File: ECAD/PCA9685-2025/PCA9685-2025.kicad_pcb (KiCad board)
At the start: 2 copper layers, 58 x 38 mm, 80 parts, among them J1 Conn_01x03, J10 Conn_01x03, J11 Conn_01x03, J12 Conn_01x03, J13 Conn_01x03, J14 Conn_01x03, J15 Conn_01x03, J16 Conn_01x03, J17 Conn_01x03, J18 Conn_01x04, J19 Conn_01x04, J2 Conn_01x02, J3 Conn_01x03, J4 Conn_01x03, J5 Conn_01x03, J6 Conn_01x03, J7 Conn_01x03, J8 Conn_01x03, J9 Conn_01x03, U1 PCA9685PW

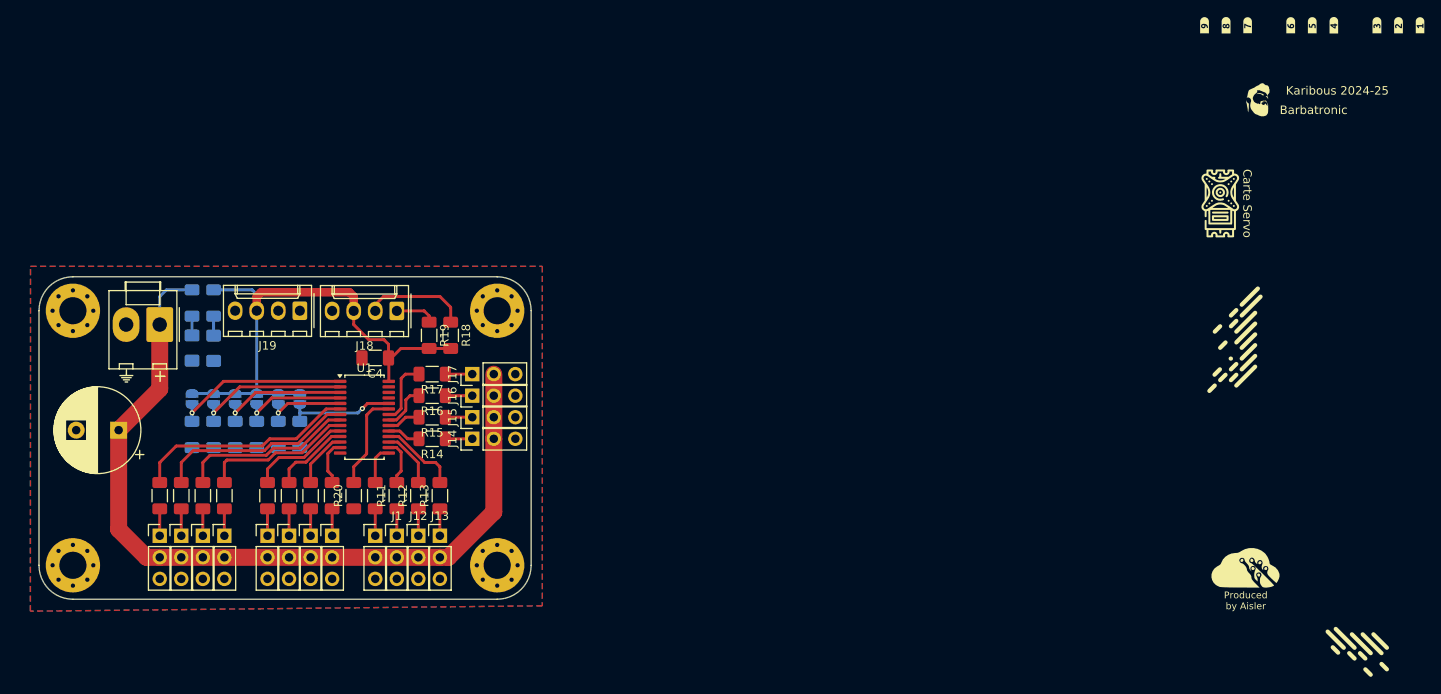
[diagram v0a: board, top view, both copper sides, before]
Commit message: finish route and update silkscreen
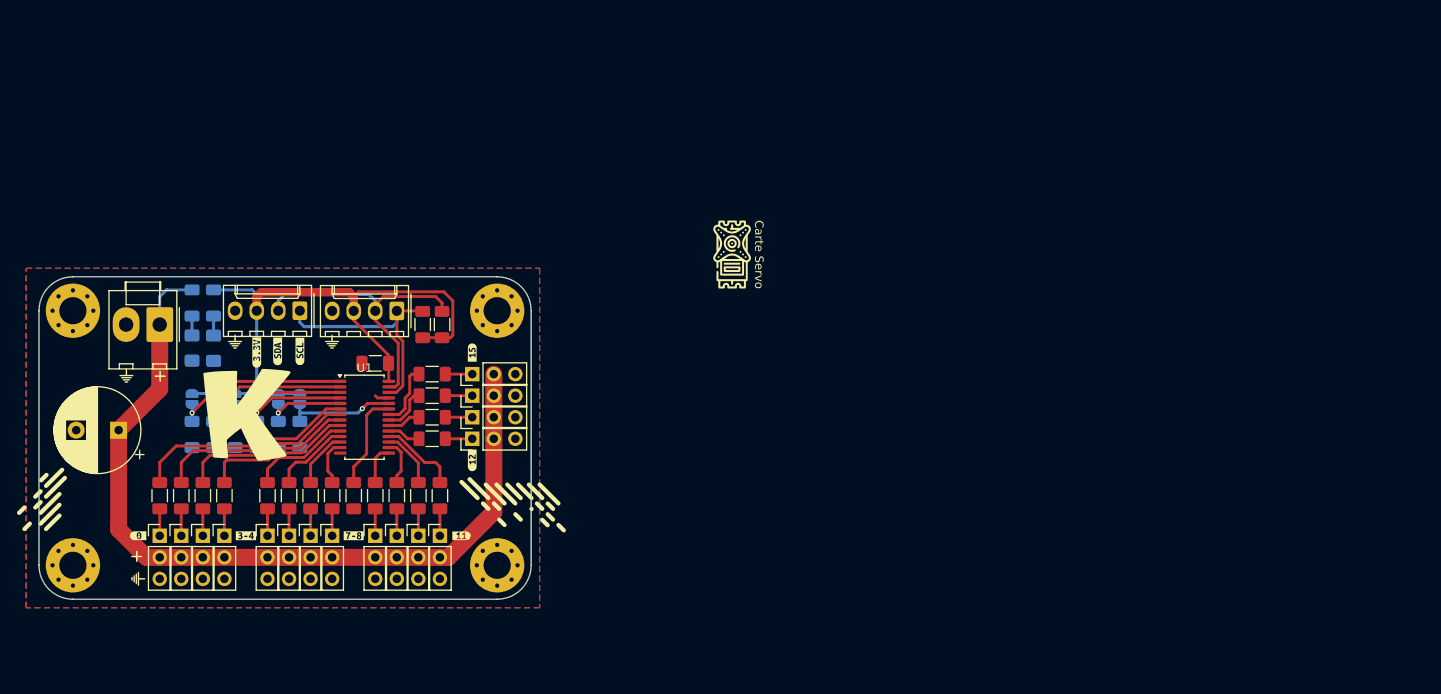
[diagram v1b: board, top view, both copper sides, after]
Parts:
- removed kibuzzard-679519F0: G***, kibuzzard-679519F0
- removed kibuzzard-67951A07: G***, kibuzzard-67951A07
- removed kibuzzard-67951A0B: G***, kibuzzard-67951A0B
- removed kibuzzard-67951A10: G***, kibuzzard-67951A10
- removed kibuzzard-67951A14: G***, kibuzzard-67951A14
- removed kibuzzard-67951A17: G***, kibuzzard-67951A17
- removed kibuzzard-67951A1B: G***, kibuzzard-67951A1B
- removed kibuzzard-67951A1E: G***, kibuzzard-67951A1E
- removed kibuzzard-67951A22: G***, kibuzzard-67951A22
- added G***: LOGO, LOGO, F.Cu at (82.5, 73.7)
- added G***: LOGO, LOGO, B.Cu at (71.1, 71.8)
- added G***: LOGO, LOGO, B.Cu at (82.5, 71.8)
- added G***: LOGO, LOGO, F.Cu at (59.7, 101.6)
- added G***: LOGO, LOGO, F.Cu at (71.1, 73.7)
- added kibuzzard-67954B90: G***, kibuzzard-67954B90, F.Cu at (97.8, 96.5)
- added kibuzzard-67954C44: G***, kibuzzard-67954C44, F.Cu at (99.1, 87.6)
- added kibuzzard-67954C4A: G***, kibuzzard-67954C4A, F.Cu at (99.1, 74.9)
- added kibuzzard-67954C57: G***, kibuzzard-67954C57, F.Cu at (59.7, 96.5)
- added kibuzzard-67954C5E: G***, kibuzzard-67954C5E, F.Cu at (72.4, 96.5)
- added kibuzzard-67954C66: G***, kibuzzard-67954C66, F.Cu at (85.1, 96.5)
- added kibuzzard-67954CC0: G***, kibuzzard-67954CC0, F.Cu at (73.7, 74.9)
- added kibuzzard-67954D1A: G***, kibuzzard-67954D1A, F.Cu at (76.1, 74.8)
- added kibuzzard-67954D30: G***, kibuzzard-67954D30, F.Cu at (78.8, 74.8)
- added kibuzzard-67954E00: G***, kibuzzard-67954E00, B.Cu at (66.0, 78.1)
- added kibuzzard-67954E2A: G***, kibuzzard-67954E2A, B.Cu at (68.6, 78.1)
- added kibuzzard-67954E2F: G***, kibuzzard-67954E2F, B.Cu at (71.1, 78.1)
- added kibuzzard-67954E34: G***, kibuzzard-67954E34, B.Cu at (73.7, 78.1)
- added kibuzzard-67954E39: G***, kibuzzard-67954E39, B.Cu at (76.2, 78.1)
- added kibuzzard-67954E3F: G***, kibuzzard-67954E3F, B.Cu at (78.7, 78.1)
- added kibuzzard-67954E7A: G***, kibuzzard-67954E7A, B.Cu at (73.7, 72.6)
- added kibuzzard-67954E7A: G***, kibuzzard-67954E7A, B.Cu at (85.1, 72.6)
- added kibuzzard-67954E99: G***, kibuzzard-67954E99, B.Cu at (76.2, 72.4)
- added kibuzzard-67954E99: G***, kibuzzard-67954E99, B.Cu at (87.6, 72.4)
- added kibuzzard-67954EA0: G***, kibuzzard-67954EA0, B.Cu at (90.2, 72.4)
- added kibuzzard-67954EA0: G***, kibuzzard-67954EA0, B.Cu at (78.7, 72.4)
- G*** (x2): moved to B.Cu
- moved G*** 120.8 mm to (80.0, 91.4), turned to 180 degrees
- moved G*** 98.7 mm to (92.2, 88.6), turned to 180 degrees
- moved G*** 57.8 mm to (129.7, 63.4)
- moved G*** 4.69 mm to (52.4, 86.4), turned to 180 degrees
- moved R18 1.63 mm to (95.5, 71.6)
- moved R19 1.48 mm to (93.2, 71.6)
- moved C4 0.64 mm to (87.6, 76.2)
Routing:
- net SCL: track 4.79 -> 28.8 mm
- net SDA: track 11.8 -> 35.7 mm
- net +3.3V: track 63.7 -> 75.0 mm
- net GND: track 0.00 -> 1.70 mm
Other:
- board text added: "Open = 0 Close = 1 Base = 0x40"
